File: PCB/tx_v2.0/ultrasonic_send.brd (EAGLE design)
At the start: 100.1 x 80 mm, 40 parts, among them J1 SBWD, J2 UART, J3 AD, J4 function, J5 pwr_5V, Q1 MMBT3904, Q2 MMBT3904, Q3 AMS1117-3.3

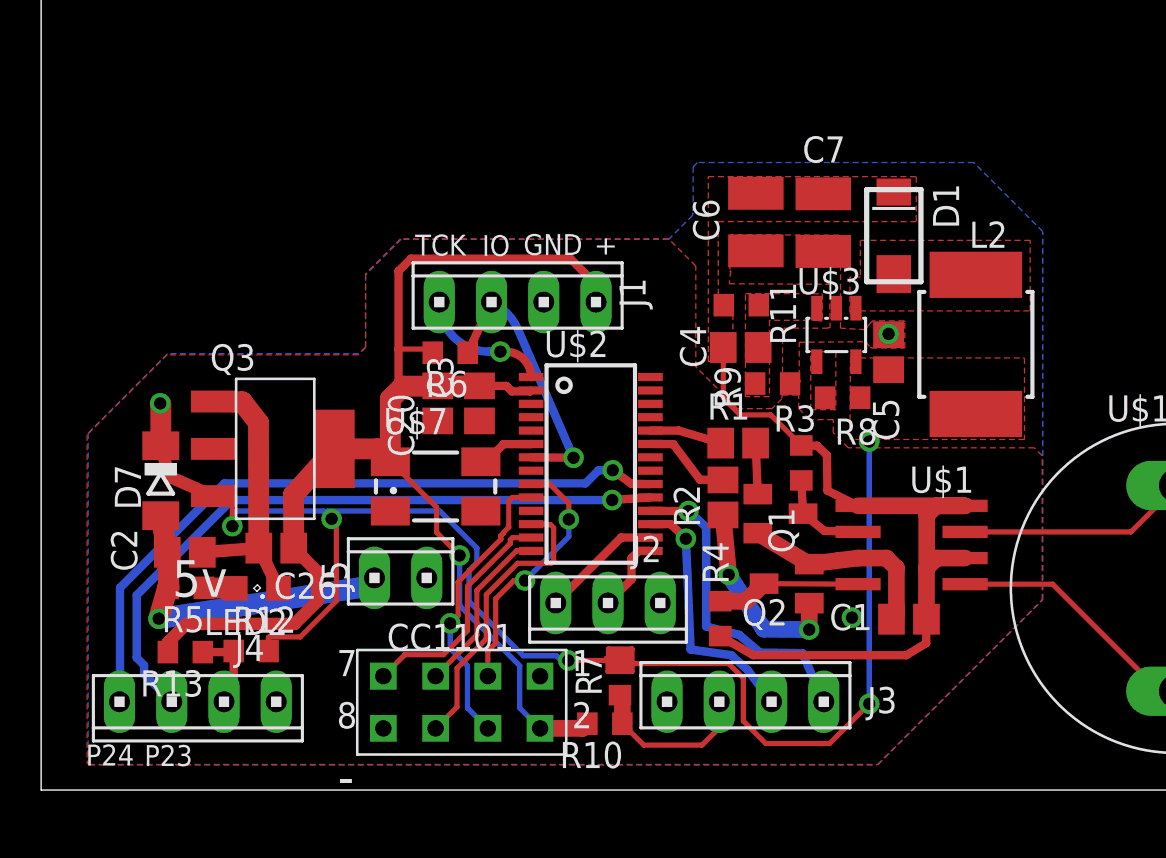
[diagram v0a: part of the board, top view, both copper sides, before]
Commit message: 2.0 PCB finished with CC1101 and reveive modules.
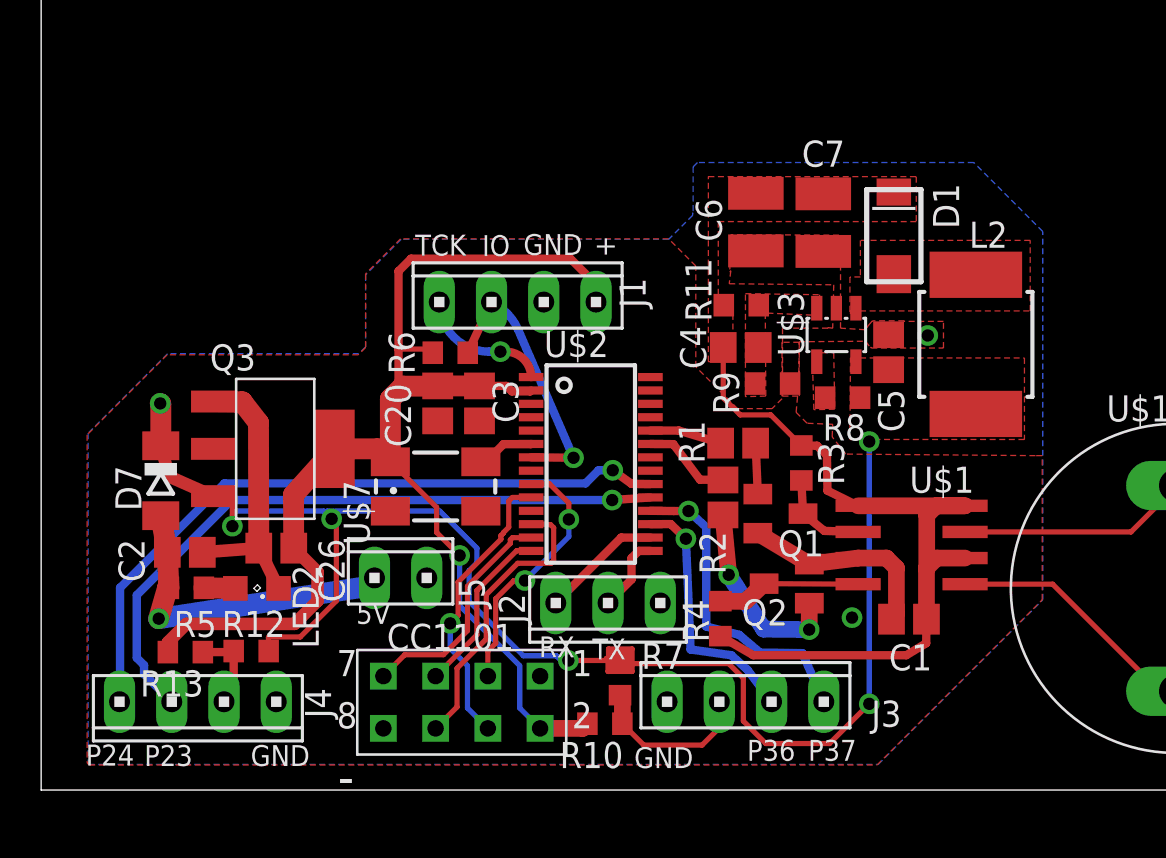
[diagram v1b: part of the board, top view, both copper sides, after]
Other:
- board text added: "5V"
- board text added: "P36"
- board text added: "P37"
- board text added: "RX"
- board text added: "TX"
- board text removed: "5v"
